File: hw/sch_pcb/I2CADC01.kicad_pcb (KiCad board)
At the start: 2 copper layers, 30 x 40.1 mm, 33 parts, among them J1 JUMP_3X2, J3 CONN_2, J4 CONN_3, J5 JUMP2_2x1, J6 JUMP2_2x1, J7 JUMP_5X2, J8 CONN_2, M1 HOLE, M2 HOLE, M3 HOLE, M4 HOLE, P1 _, P2 _, U1 LTC2485

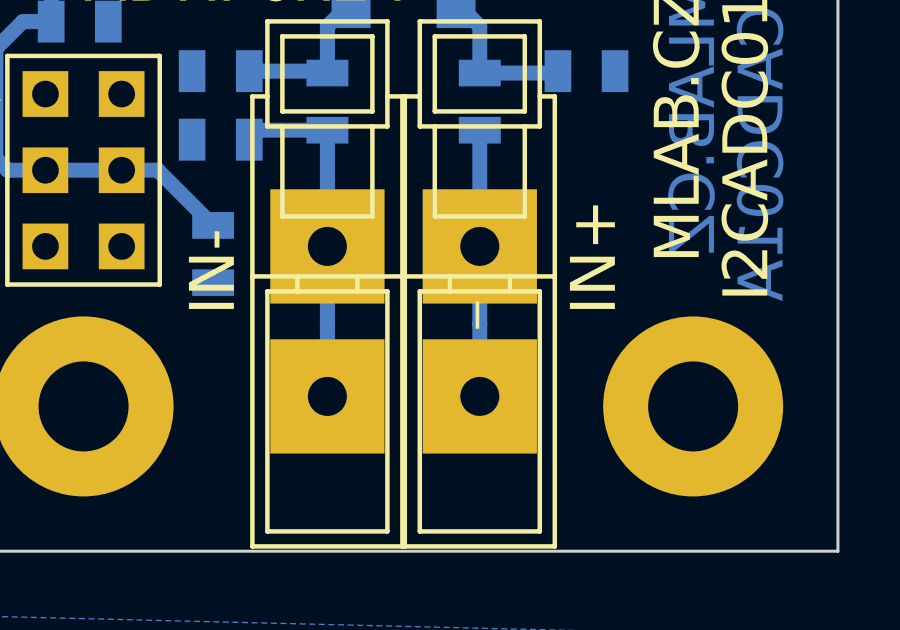
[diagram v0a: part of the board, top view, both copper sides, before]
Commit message: Adding assets update title block.
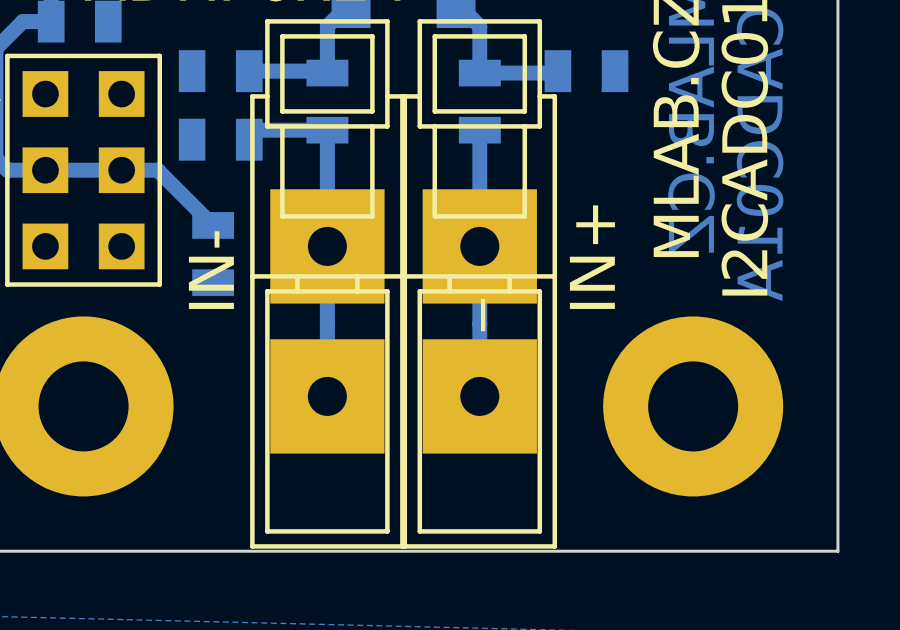
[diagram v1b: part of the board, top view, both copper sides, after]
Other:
- net class Default removed
